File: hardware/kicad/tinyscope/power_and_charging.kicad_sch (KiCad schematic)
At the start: 44 parts

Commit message: feat: hardware: Add tinyscope kicad project. Create flow diagram for MCUs sheet. Adds decoupling caps for STM32H743
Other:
- title: (none) -> Power Input & Charging
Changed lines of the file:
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@@
 (kicad_sch (version 20230121) (generator eeschema)
   (paper "A3")
+  (title_block
+    (title "Power Input & Charging")
+    (rev "v0.1")
+  )
   (junction (at 215.9 48.26) (diameter 0) (color 0 0 0 0)
   )

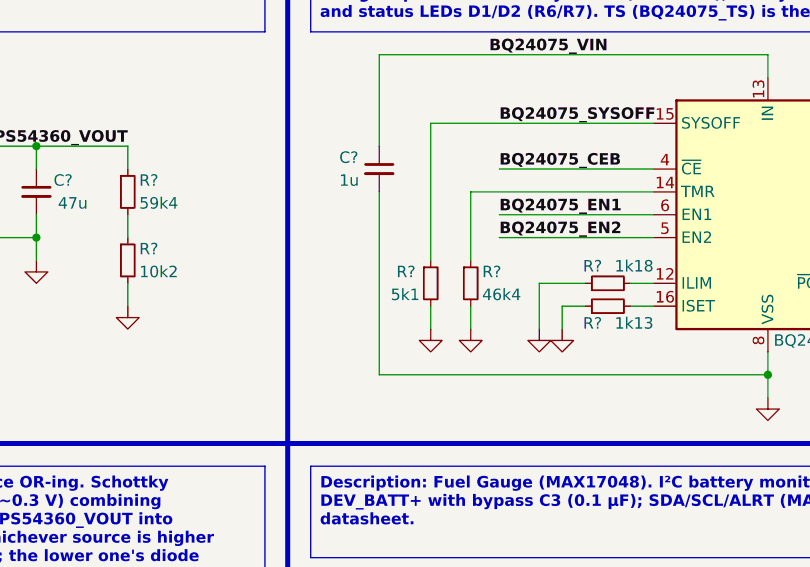
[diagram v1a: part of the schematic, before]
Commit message: feat: hardware: Adds blue led mosfet driver for MDBT50Q
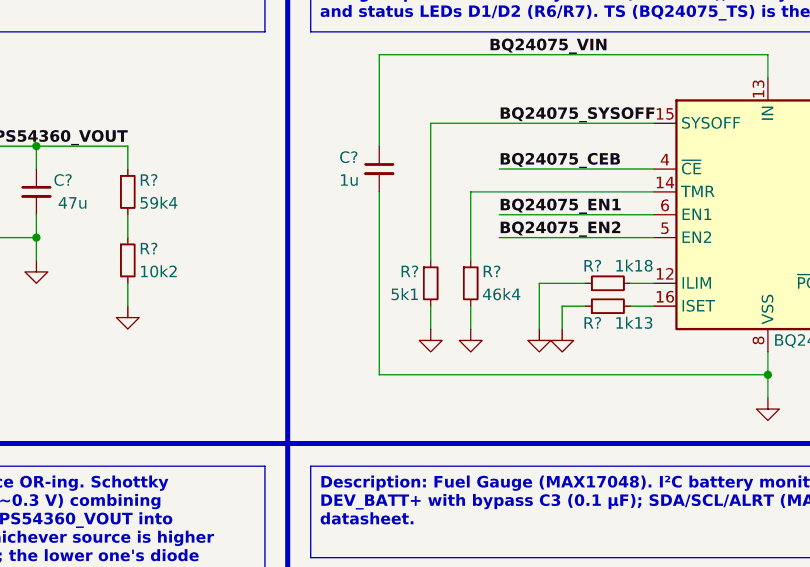
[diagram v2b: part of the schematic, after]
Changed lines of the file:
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@@
   (symbol (lib_id "Device:R_Small") (at 292.735 63.5 0) (unit 1)
     (in_bom yes) (on_board yes) (dnp no)
-    (property "Reference" "R?" (at 288.925 62.23 0)
-      (effects (font (size 1.27 1.27)) (justify left))
+    (property "Reference" "R?" (at 291.465 62.23 0)
+      (effects (font (size 1.27 1.27)) (justify right))
     )
-    (property "Value" "5k1" (at 288.29 64.77 0)
-      (effects (font (size 1.27 1.27)) (justify left))
+    (property "Value" "5k1" (at 291.465 64.77 0)
+      (effects (font (size 1.27 1.27)) (justify right))
     )
     (property "Footprint" "" (at 292.735 63.5 0)
